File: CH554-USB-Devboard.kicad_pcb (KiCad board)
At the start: 2 copper layers, 22.9 x 35.6 mm, 22 parts, among them J1 Conn_01x10_Male, J2 Conn_01x10_Male, J3 USB_B_Micro, SW1 SW_Push, SW2 SW_Push, U1 CH552T, U2 CH552G, Y1 Crystal

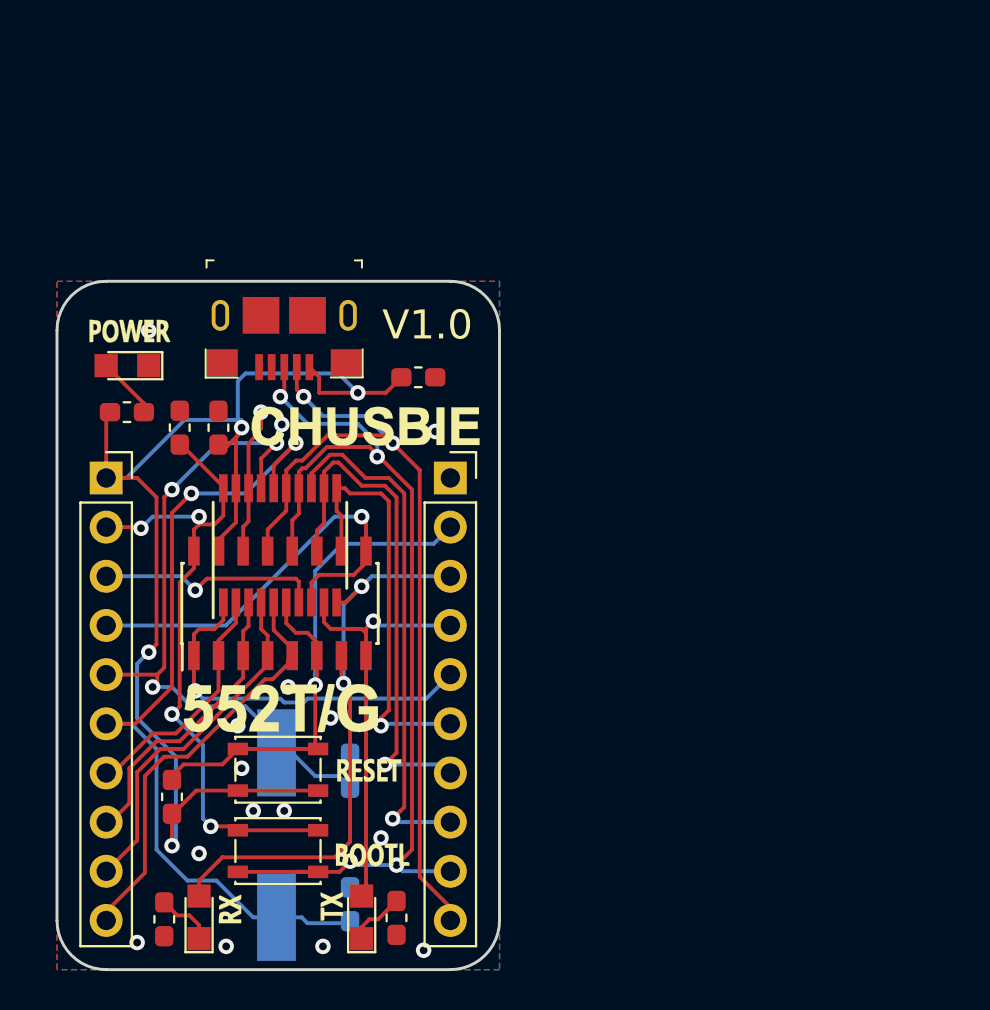
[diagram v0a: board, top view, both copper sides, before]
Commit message: schematic complete started to route
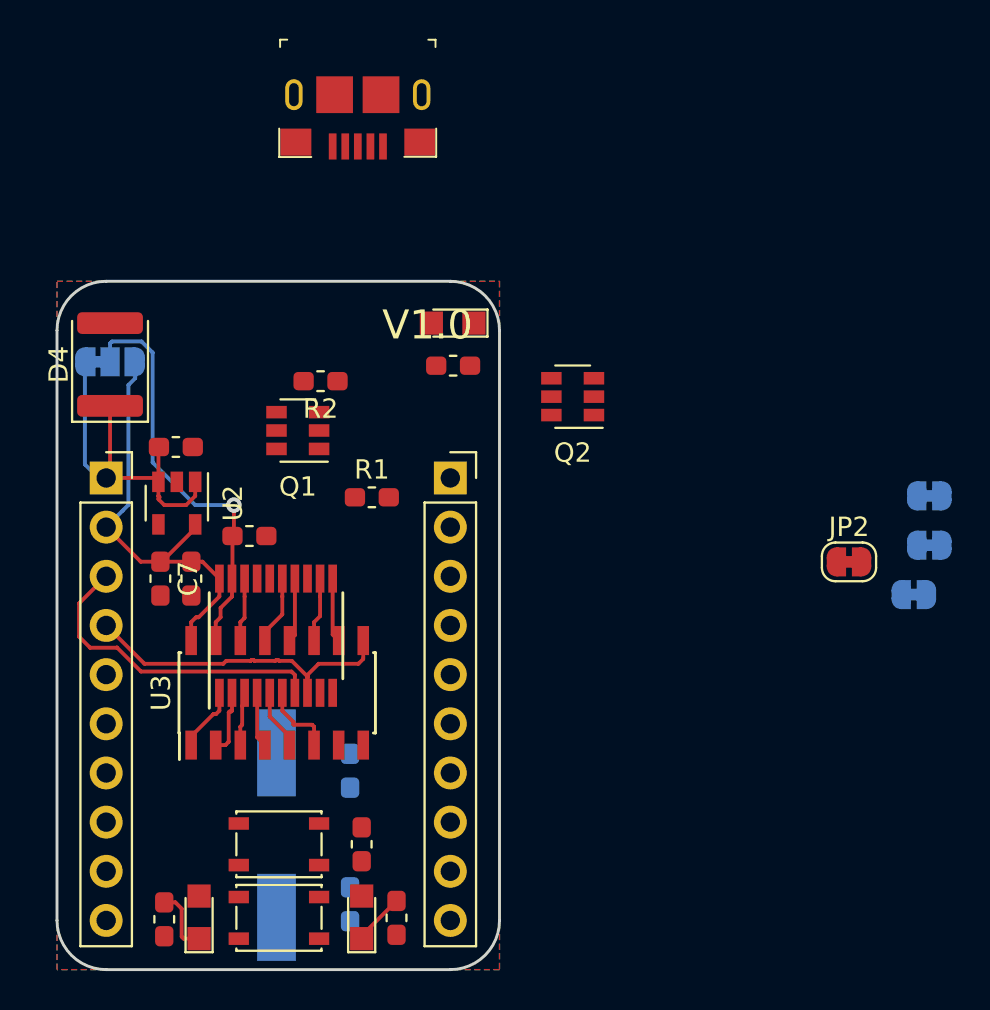
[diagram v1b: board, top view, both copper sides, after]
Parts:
- removed G***: LOGO, ArtandSilks:frontsilk
- removed G***: LOGO, ArtandSilks:rearsilk
- added C7: 100nF, Capacitor_SMD:C_0603_1608Metric_Pad1.05x0.95mm_HandSolder, F.Cu at (79.0, 81.4)
- added D4: SMBJ58A+, Diode_SMD:D_1812_4532Metric, F.Cu at (76.4, 70.3)
- added JP1: Jumper_3_Bridged12, Jumper:SolderJumper-3_P1.3mm_Bridged12_RoundedPad1.0x1.5mm_NumberLabels, B.Cu at (76.4, 70.2)
- added JP2: Jumper_NC_Small, Jumper:SolderJumper-2_P1.3mm_Bridged_RoundedPad1.0x1.5mm, F.Cu at (114.6, 80.5)
- added JP3: Jumper_NC_Small, Jumper:SolderJumper-2_P1.3mm_Bridged_RoundedPad1.0x1.5mm, B.Cu at (118.7, 79.7)
- added JP4: Jumper_NC_Small, Jumper:SolderJumper-2_P1.3mm_Bridged_RoundedPad1.0x1.5mm, B.Cu at (117.9, 82.2)
- added JP5: Jumper_NC_Small, Jumper:SolderJumper-2_P1.3mm_Bridged_RoundedPad1.0x1.5mm, B.Cu at (118.7, 77.1)
- added Q1: CPH6337, TO_SOT_Packages_SMD:SOT-23-6, F.Cu at (86.1, 73.8)
- added Q2: CPH6337, TO_SOT_Packages_SMD:SOT-23-6, F.Cu at (100.3, 72.0)
- added R1: 10k, Resistor_SMD:R_0603_1608Metric_Pad1.05x0.95mm_HandSolder, F.Cu at (89.9, 77.2)
- added R2: 10k, Resistor_SMD:R_0603_1608Metric_Pad1.05x0.95mm_HandSolder, F.Cu at (87.3, 71.2)
- added U3: CH554G, Housings_SOIC:SOIC-16_3.9x9.9mm_Pitch1.27mm, F.Cu at (85.0, 87.3)
- C5, C6: value 100uF -> 15pF
- J3: value USB_B_Micro -> USB_C_Receptacle
- U1: value CH552T -> CH554T
- U2: value CH552G -> MIC5504-3.3YM5; footprint Housings_SOIC:SOIC-16_3.9x9.9mm_Pitch1.27mm -> Package_TO_SOT_SMD:SOT-23-5
- moved R5 17.0 mm to (94.1, 70.4)
- moved D3 16.9 mm to (94.1, 68.2)
- moved C4 13.0 mm to (79.8, 74.6)
- moved J3 12.0 mm to (89.2, 56.4)
- moved C3 10.1 mm to (89.4, 95.1)
- moved C2 7.82 mm to (80.6, 81.4), turned to 270 degrees
- moved U2 7.43 mm to (79.8, 77.5), turned to 270 degrees
- moved C1 5.82 mm to (83.6, 79.2), turned to 0 degrees
- moved U1 4.67 mm to (85.0, 84.3)
- moved SW2 3.85 mm to (85.1, 95.1)
- moved SW1 3.45 mm to (85.1, 98.9)
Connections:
- C1 pad 1: VCC -> /VSYS
- J3 pad 1: VCC -> (no net)
- J3 pad 2: /P3.7 -> (no net)
- J3 pad 3: /P3.6 -> (no net)
- J3 pad 4: Net-(J3-Pad4) -> (no net)
- J3 pad 5: GND -> (no net)
- J3 pad SH: GND -> (no net)
- U1 pad 19: VCC -> /VSYS
- U2 pad 1: /P3.2 -> VCC
- U2 pad 2: /P1.4 -> GND
- U2 pad 3: /P1.5 -> VCC
- U2 pad 4: /P1.6 -> Net-(U2-Pad4)
- U2 pad 5: /P1.7 -> +3V3
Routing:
- net /P3.6: track 52.8 -> 3.32 mm, vias 4 -> 0
- net VCC: track 67.3 -> 19.0 mm, vias 4 -> 0
- net /P1.3: track 43.6 -> 0.00 mm, vias 2 -> 0
- net /P3.7: track 44.1 -> 3.57 mm, vias 2 -> 0
- net /P1.2: track 35.1 -> 0.00 mm, vias 3 -> 0
- net /P3.0: track 31.2 -> 0.00 mm, vias 2 -> 0
- net /RESET: track 31.1 -> 3.94 mm, vias 1 -> 0
- net /P3.5: track 26.9 -> 0.00 mm, vias 1 -> 0
- net /P3.4: track 26.6 -> 3.33 mm, vias 1 -> 0
- net /P3.1: track 23.1 -> 0.00 mm, vias 1 -> 0
- net /VSYS: track 0.00 -> 21.6 mm, vias 0 -> 1
- net /P1.7: track 21.7 -> 3.12 mm
- net /P3.3: track 21.7 -> 3.33 mm, vias 1 -> 0
- net /P3.2: track 19.7 -> 3.38 mm, vias 1 -> 0
- net /P1.6: track 18.2 -> 2.87 mm
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
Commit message: more routing
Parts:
- JP2: moved to B.Cu
- moved JP5 37.1 mm to (82.3, 69.6)
- moved JP4 37.1 mm to (82.4, 71.7)
- moved JP3 34.2 mm to (84.8, 75.2)
- moved JP2 26.3 mm to (88.8, 75.1)
- moved Q2 15.8 mm to (84.8, 75.1), turned to 90 degrees
- moved Q1 2.71 mm to (88.5, 75.1), turned to 90 degrees
- moved R2 1.77 mm to (88.6, 72.4), turned to 0 degrees
- moved R1 1.62 mm to (88.4, 77.8)
- moved C3 0.71 mm to (88.7, 95.0)
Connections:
- C3 pad 1: VCC -> /VSYS
- D1 pad 2: /P3.0 -> /P3.1
- D2 pad 2: /P3.1 -> /P3.0
- SW2 pad 2: VCC -> /VSYS
- U3 pad 7: /P3.0 -> /P3.1
- U3 pad 8: /P3.1 -> /P3.0
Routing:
- net /P3.6: track 3.32 -> 62.6 mm, vias 0 -> 2
- net /P3.7: track 3.57 -> 47.8 mm, vias 0 -> 1
- net /P1.3: track 0.00 -> 38.9 mm, vias 0 -> 1
- net /P1.5: track 2.79 -> 32.9 mm
- net /P3.1: track 0.00 -> 28.7 mm, vias 0 -> 1
- net /RESET: track 3.94 -> 30.7 mm, vias 0 -> 2
- net /P1.4: track 3.39 -> 27.1 mm, vias 0 -> 1
- net /P1.2: track 0.00 -> 23.4 mm, vias 0 -> 2
- net /P3.3: track 3.33 -> 25.8 mm, vias 0 -> 2
- net /VSYS: track 21.6 -> 43.7 mm, vias 1 -> 3
- net /P3.5: track 0.00 -> 21.9 mm, vias 0 -> 1
- net +3V3: track 22.7 -> 43.9 mm, vias 0 -> 2
- net /P3.0: track 0.00 -> 20.8 mm, vias 0 -> 1
- net /P3.4: track 3.33 -> 21.5 mm, vias 0 -> 1
- net /P1.7: track 3.12 -> 19.2 mm
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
